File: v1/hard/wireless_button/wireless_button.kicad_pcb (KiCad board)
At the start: 2 copper layers, 82 x 56 mm, 21 parts, among them J1 USB_B_Micro, J2 RJ12, J3 Conn_01x01_Female, Q1 Q_PMOS_GSD, SW1 SW_Push, U1 STM32F103C8Tx, U2 CC1101_MOD, U3 OLED_0.91

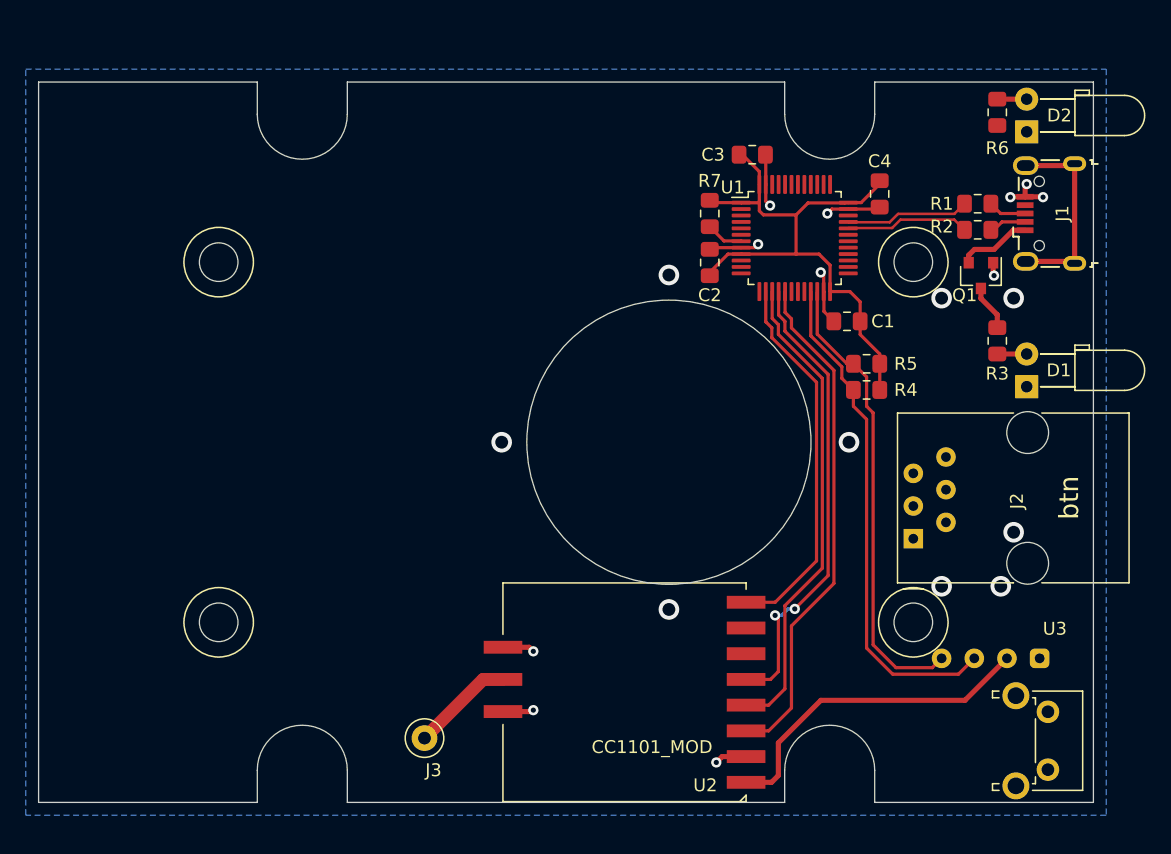
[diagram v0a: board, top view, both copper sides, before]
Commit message: Wireless button PCB updates. - added EEPROM - added connector for "pull-up" opto output - added overvoltage protection zener between source and gate of reverse protecting MOSFETs
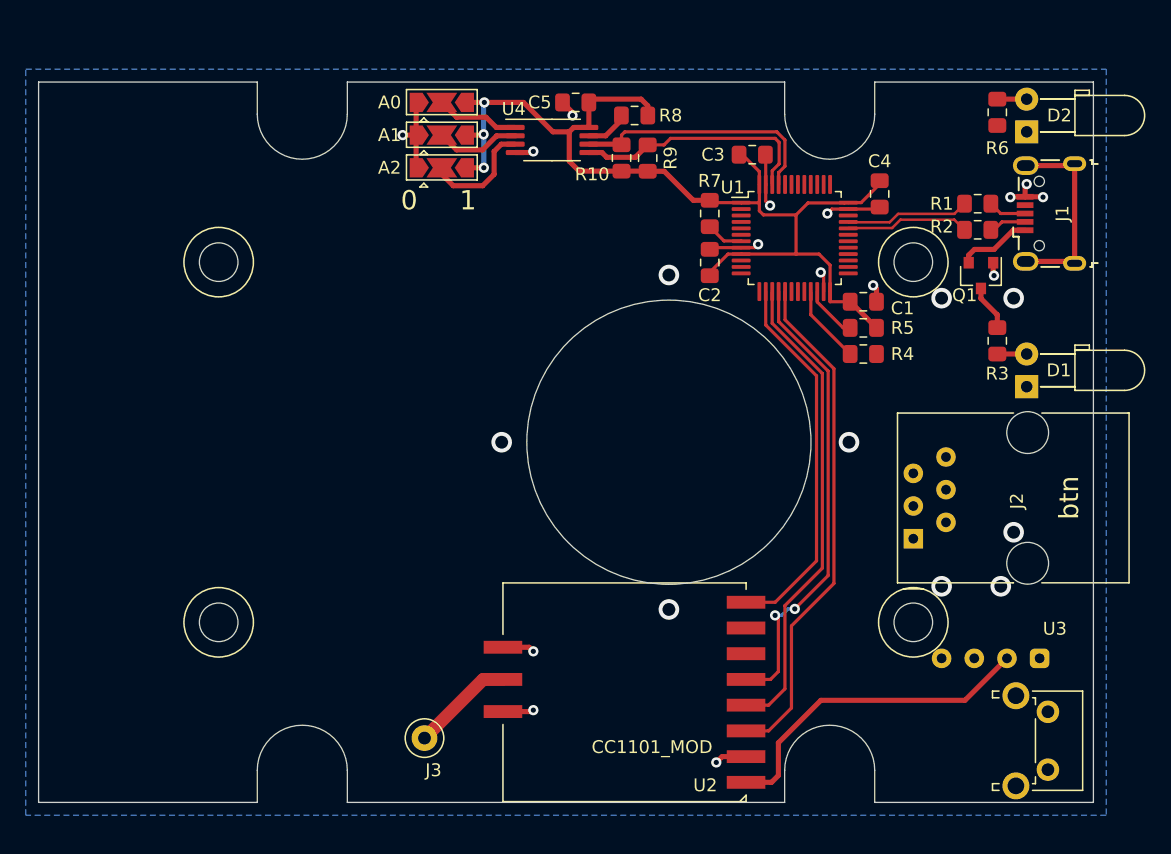
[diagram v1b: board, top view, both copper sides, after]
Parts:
- added C5: 0.1uF, Resistor_SMD:R_0805_2012Metric_Pad1.15x1.40mm_HandSolder, F.Cu at (100.8, 73.6)
- added JP1: A0, Jumper:SolderJumper-3_P2.0mm_Open_TrianglePad1.0x1.5mm, F.Cu at (90.3, 73.6)
- added JP2: A1, Jumper:SolderJumper-3_P2.0mm_Open_TrianglePad1.0x1.5mm, F.Cu at (90.3, 76.1)
- added JP3: A2, Jumper:SolderJumper-3_P2.0mm_Open_TrianglePad1.0x1.5mm, F.Cu at (90.3, 78.7)
- added R10: 4k7, Resistor_SMD:R_0805_2012Metric_Pad1.15x1.40mm_HandSolder, F.Cu at (104.3, 77.9)
- added R8: 4k7, Resistor_SMD:R_0805_2012Metric_Pad1.15x1.40mm_HandSolder, F.Cu at (105.3, 74.6)
- added R9: 4k7, Resistor_SMD:R_0805_2012Metric_Pad1.15x1.40mm_HandSolder, F.Cu at (106.3, 77.9)
- added U4: 24LC128, Package_SO:TSSOP-8_4.4x3mm_P0.65mm, F.Cu at (98.9, 76.5)
- moved R4 2.81 mm to (123.1, 93.1)
- moved R5 2.81 mm to (123.1, 91.1)
- moved C1 1.98 mm to (123.1, 89.1), turned to 0 degrees
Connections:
- U1 pad 45: Net-(U1-Pad45) -> /MEM_SCL
- U1 pad 46: Net-(U1-Pad46) -> /MEM_SDA
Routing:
- net +3V3: track 71.5 -> 106.9 mm, vias 0 -> 3
- net /OLED_SCL: track 39.2 -> 6.12 mm
- net /OLED_SDA: track 35.9 -> 4.20 mm
- net /MEM_SCL: track 0.00 -> 20.0 mm
- net /MEM_SDA: track 0.00 -> 19.2 mm
- net /MEM_A2: track 0.00 -> 8.96 mm
- net GND: track 28.6 -> 36.2 mm, vias 20 -> 24
- net /MEM_A1: track 0.00 -> 6.63 mm
- net /MEM_A0: track 0.00 -> 6.51 mm
- net /WP: track 0.00 -> 3.39 mm
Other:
- board text added: "0"
- board text added: "1"

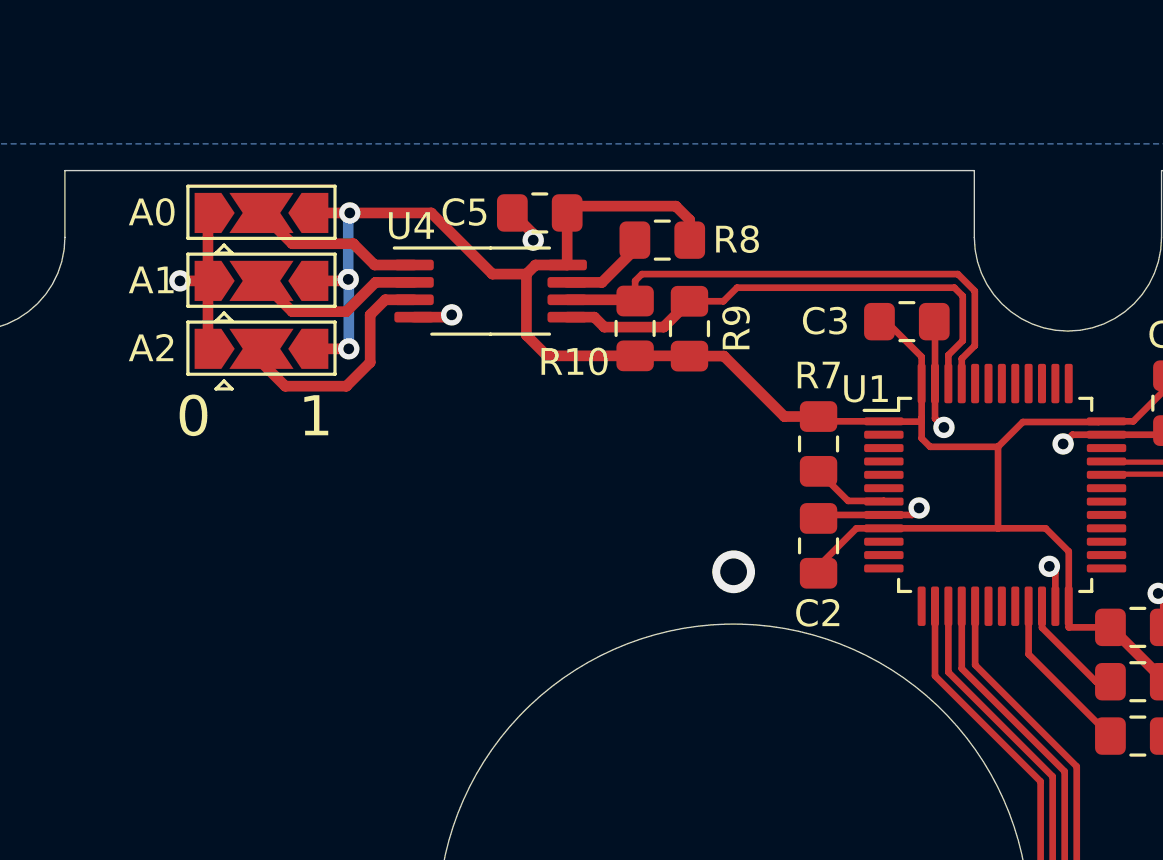
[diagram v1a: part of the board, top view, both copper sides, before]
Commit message: !!! Important. This is last commit before changing case from 1593L (aka BMD 60035) to G01B. !!! Many additions to wireless button. Came to conclusion that box is too small, mostly because of cuts on board sides. Also desided to drop idea powering from Li-batteriies and change to non rechangable +9V.
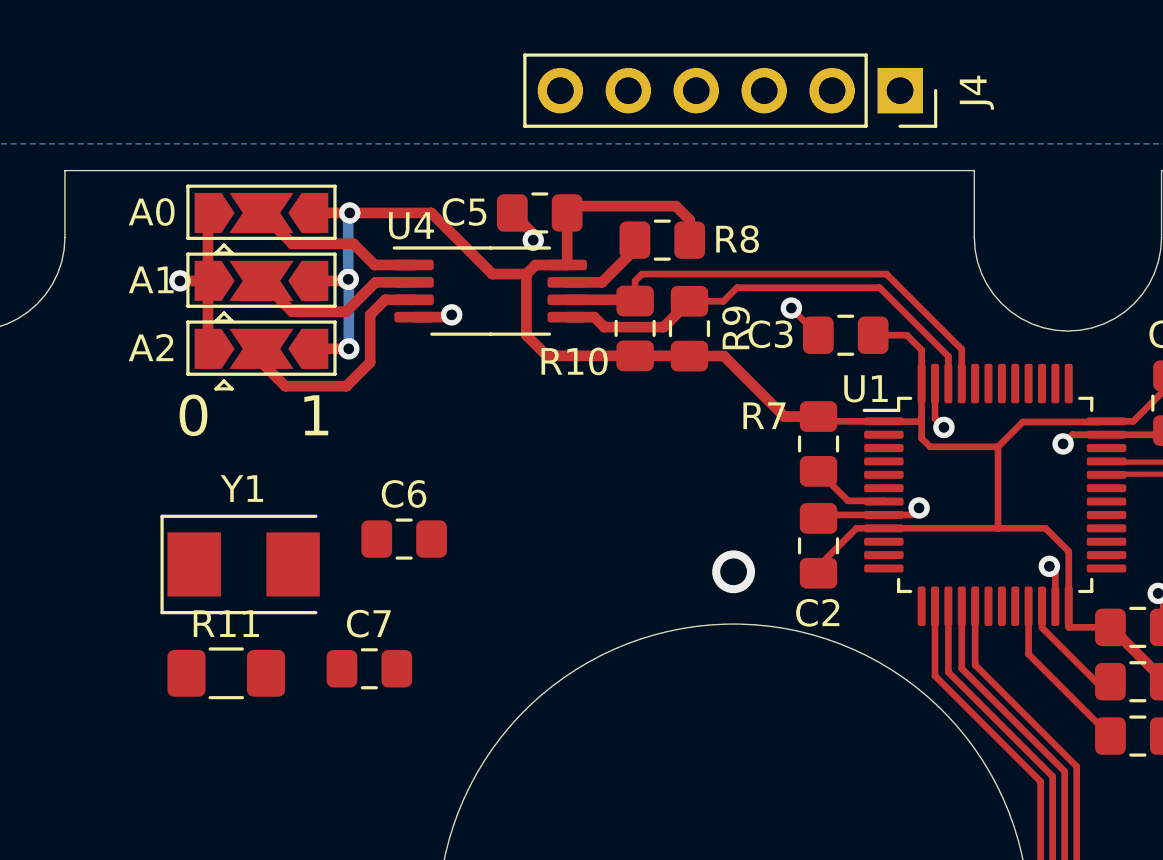
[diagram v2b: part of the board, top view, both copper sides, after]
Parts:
- added C6: 22pF, Resistor_SMD:R_0805_2012Metric_Pad1.15x1.40mm_HandSolder, F.Cu at (95.7, 85.8)
- added C7: 22pF, Resistor_SMD:R_0805_2012Metric_Pad1.15x1.40mm_HandSolder, F.Cu at (94.4, 90.6)
- added J4: Conn_01x06_Male, Connector_PinSocket_2.54mm:PinSocket_1x06_P2.54mm_Vertical, F.Cu at (114.2, 69.0)
- added R11: 1M, Resistor_SMD:R_1206_3216Metric_Pad1.42x1.75mm_HandSolder, F.Cu at (89.0, 90.8)
- added Y1: 8MHz, Crystal:Crystal_SMD_5032-2Pin_5.0x3.2mm, F.Cu at (89.7, 86.7)
- R7: value 47k -> 100k
- moved C3 2.34 mm to (112.2, 78.2), turned to 180 degrees
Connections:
- net /~RES renamed /NRST
- U1 pad 34: Net-(U1-Pad34) -> /SWDIO
- U1 pad 37: Net-(U1-Pad37) -> /SWCLK
- U1 pad 5: Net-(U1-Pad5) -> /OSCIN
- U1 pad 6: Net-(U1-Pad6) -> /OSCOUT
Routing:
- net /MEM_SDA: track 19.2 -> 17.1 mm
- net /MEM_SCL: track 20.0 -> 18.1 mm
- net GND: track 36.2 -> 35.3 mm, vias 24 -> 25

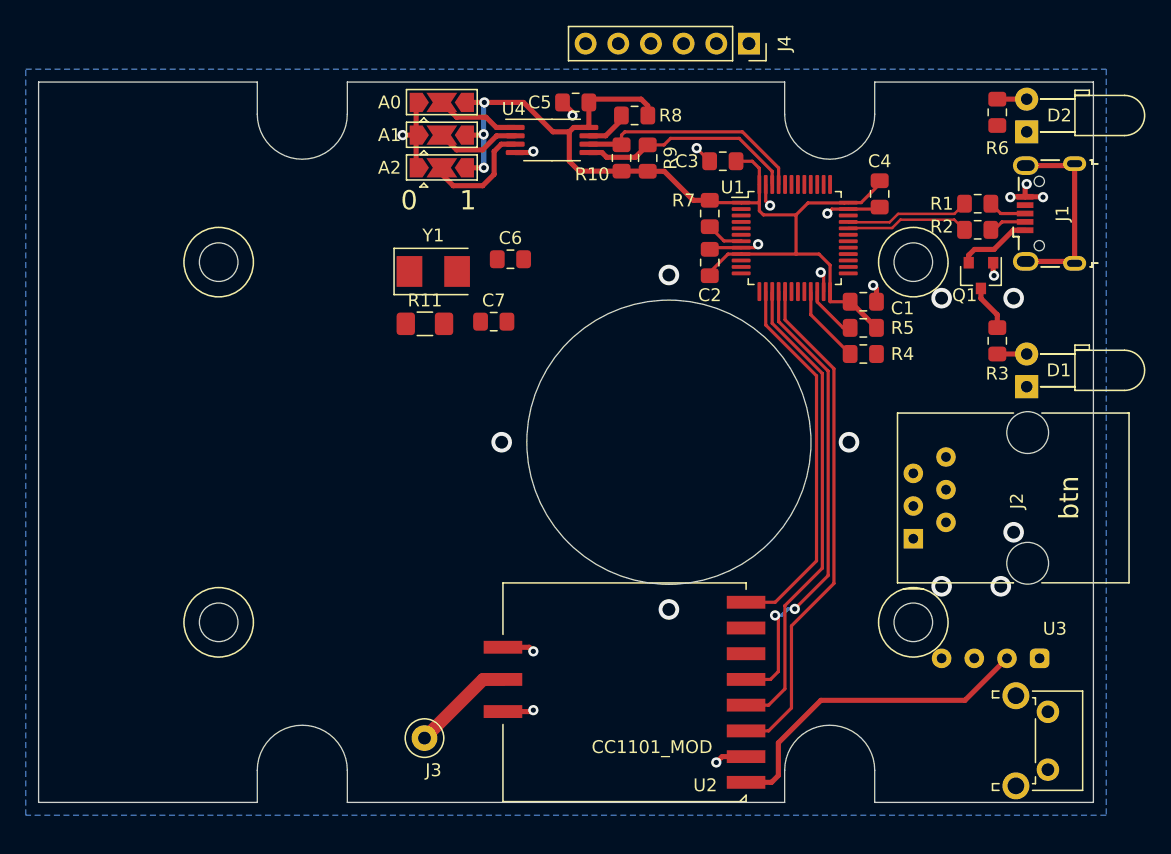
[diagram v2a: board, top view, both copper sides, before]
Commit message: Finished wireless button PCB v0.1. Added step-down converter to 3.3V from wide range input voltage. May contain serios mistakes, board is a prototype only.
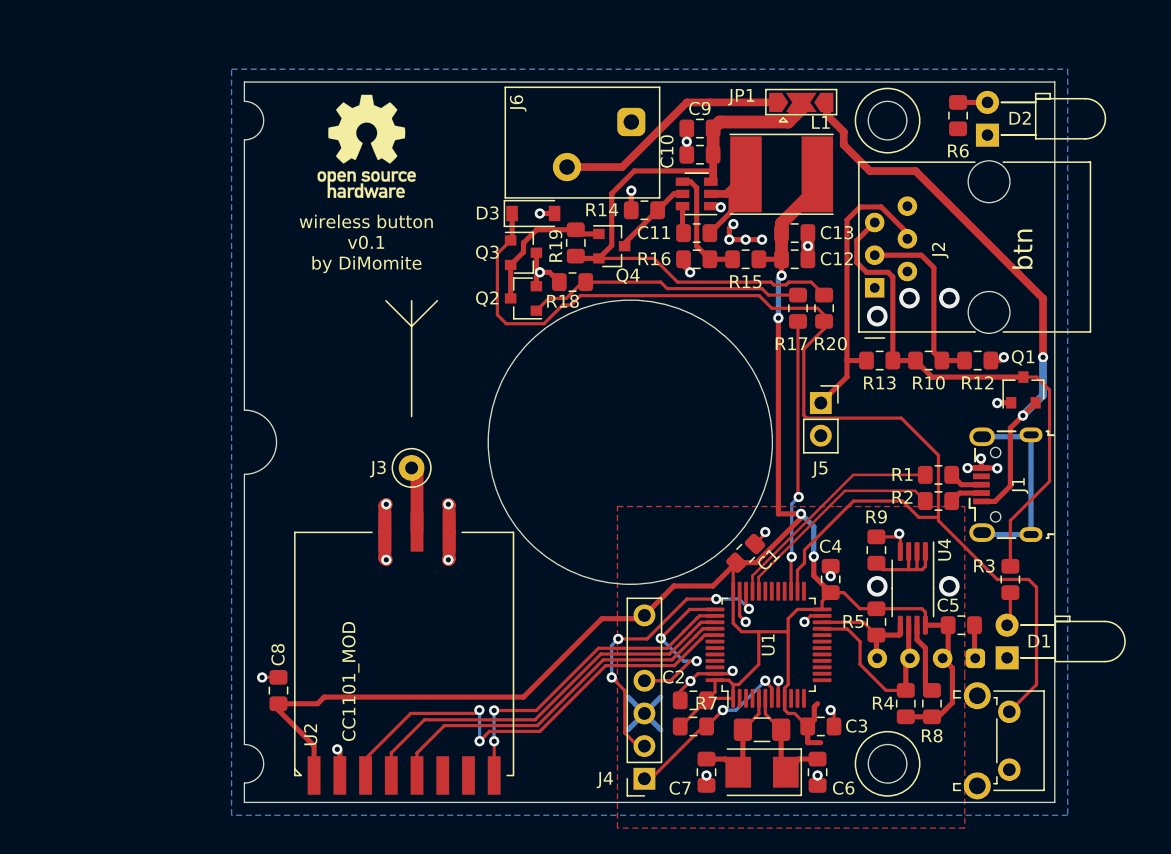
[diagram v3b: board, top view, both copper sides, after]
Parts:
- removed JP2: A1, Jumper:SolderJumper-3_P2.0mm_Open_TrianglePad1.0x1.5mm
- removed JP3: A2, Jumper:SolderJumper-3_P2.0mm_Open_TrianglePad1.0x1.5mm
- added C10: 10uF, Resistor_SMD:R_0805_2012Metric_Pad1.15x1.40mm_HandSolder, F.Cu at (110.4, 77.6)
- added C11: 0.1uF, Resistor_SMD:R_0805_2012Metric_Pad1.15x1.40mm_HandSolder, F.Cu at (110.2, 83.7)
- added C12: 22uF, Resistor_SMD:R_0805_2012Metric_Pad1.15x1.40mm_HandSolder, F.Cu at (117.8, 85.8)
- added C13: 22uF, Resistor_SMD:R_0805_2012Metric_Pad1.15x1.40mm_HandSolder, F.Cu at (117.8, 83.7)
- added C8: 0.1uF, Resistor_SMD:R_0805_2012Metric_Pad1.15x1.40mm_HandSolder, F.Cu at (77.6, 119.3)
- added C9: 10uF, Resistor_SMD:R_0805_2012Metric_Pad1.15x1.40mm_HandSolder, F.Cu at (110.4, 75.6)
- added D3: 4.8V, Diode_SMD:D_SOD-123, F.Cu at (97.5, 82.2)
- added J5: Conn_01x02_Female, Connector_PinSocket_2.54mm:PinSocket_1x02_P2.54mm_Vertical, F.Cu at (119.8, 97.0)
- added J6: Conn_01x02_Female, brbuttonsystem:Wago 250-3.5-2P-2, F.Cu at (105.1, 75.1)
- added L1: 4.7uH, Inductor_SMD:L_Taiyo-Yuden_NR-60xx_HandSoldering, F.Cu at (116.8, 79.2)
- added Q2: IRLML2803, Package_TO_SOT_SMD:SOT-23, F.Cu at (96.7, 88.8)
- added Q3: TP0610T, Package_TO_SOT_SMD:SOT-23, F.Cu at (96.7, 85.3)
- added Q4: TP0610T, Package_TO_SOT_SMD:SOT-23, F.Cu at (103.6, 84.8)
- added R12: 10k, Resistor_SMD:R_0805_2012Metric_Pad1.15x1.40mm_HandSolder, F.Cu at (132.0, 93.7)
- added R13: 4k7, Resistor_SMD:R_0805_2012Metric_Pad1.15x1.40mm_HandSolder, F.Cu at (124.4, 93.7)
- added R14: 100k, Resistor_SMD:R_0805_2012Metric_Pad1.15x1.40mm_HandSolder, F.Cu at (106.1, 82.0)
- added R15: 33.2k 1%, Resistor_SMD:R_0805_2012Metric_Pad1.15x1.40mm_HandSolder, F.Cu at (114.0, 85.8)
- added R16: 10k 1%, Resistor_SMD:R_0805_2012Metric_Pad1.15x1.40mm_HandSolder, F.Cu at (110.2, 85.8)
- added R17: 100k, Resistor_SMD:R_0805_2012Metric_Pad1.15x1.40mm_HandSolder, F.Cu at (118.0, 89.6)
- added R18: 100k, Resistor_SMD:R_0805_2012Metric_Pad1.15x1.40mm_HandSolder, F.Cu at (100.5, 87.6)
- added R19: 100k, Resistor_SMD:R_0805_2012Metric_Pad1.15x1.40mm_HandSolder, F.Cu at (100.8, 84.5)
- added R20: 10k, Resistor_SMD:R_0805_2012Metric_Pad1.15x1.40mm_HandSolder, F.Cu at (120.1, 89.6)
- added REF**: OSHW-Logo_7.5x8mm_SilkScreen, Symbol:OSHW-Logo_7.5x8mm_SilkScreen, F.Cu at (84.5, 77.0)
- added U5: TPS562200, Package_TO_SOT_SMD:SOT-23-6, F.Cu at (110.2, 80.7)
- JP1: value A0 -> Jumper_3_Bridged12
- R10, R9: value 4k7 -> 10k
- moved J4 57.7 mm to (106.1, 126.2), turned to 180 degrees
- moved R8 51.2 mm to (128.4, 120.3), turned to 90 degrees
- moved C5 50.5 mm to (130.7, 114.2), turned to 0 degrees
- moved Y1 46.6 mm to (115.2, 125.7), turned to 180 degrees
- moved C6 46.5 mm to (119.6, 125.7), turned to 270 degrees
- moved U4 44.7 mm to (127.0, 111.4), turned to 270 degrees
- moved C3 44.6 mm to (119.8, 122.1), turned to 0 degrees
- moved R11 41.0 mm to (115.2, 122.4)
- moved R7 39.9 mm to (109.9, 122.1), turned to 180 degrees
- moved C7 38.7 mm to (110.9, 125.7), turned to 270 degrees
- moved R9 35.3 mm to (124.1, 108.4), turned to 270 degrees
- moved U2 35.1 mm to (78.9, 125.9), turned to 90 degrees
- moved C2 34.1 mm to (109.9, 120.1), turned to 180 degrees
- moved U1 31.7 mm to (115.7, 115.7), turned to 90 degrees
- moved C4 30.2 mm to (120.6, 110.7), turned to 90 degrees
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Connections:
- net Net-(D1-Pad2) renamed /Reverse
- J2 pad 2: Net-(J2-Pad2) -> GND
- J2 pad 3: Net-(J2-Pad3) -> /MiddlePoint
- J2 pad 4: Net-(J2-Pad4) -> /ButtonPoint
- J2 pad 5: GND -> /PowInButt
- JP1 pad 1: GND -> +BATT
- JP1 pad 2: /MEM_A0 -> Net-(C10-Pad1)
- JP1 pad 3: +3V3 -> +5V
- Q1 pad 3: Net-(J2-Pad2) -> /PowInButt
- R10 pad 1: +3V3 -> /MiddlePoint
- R10 pad 2: /MEM_SCL -> /PowInButt
- R3 pad 1: Net-(J2-Pad2) -> /PowInButt
- R9 pad 1: +3V3 -> GND
- R9 pad 2: /MEM_SDA -> Net-(R9-Pad2)
- U1 pad 14: /WL_CS -> Net-(U1-Pad14)
- U1 pad 15: /WL_SCK -> Net-(U1-Pad15)
- U1 pad 16: /WL_MISO -> Net-(U1-Pad16)
- U1 pad 17: /WL_MOSI -> Net-(U1-Pad17)
- U1 pad 26: Net-(U1-Pad26) -> /power_switch
- U1 pad 27: Net-(U1-Pad27) -> /EN_PIN
- U1 pad 38: Net-(U1-Pad38) -> /WL_CS
- U1 pad 39: Net-(U1-Pad39) -> /WL_SCK
- U1 pad 40: Net-(U1-Pad40) -> /WL_MISO
- U1 pad 41: Net-(U1-Pad41) -> /WL_MOSI
- U4 pad 1: /MEM_A0 -> Net-(R9-Pad2)
- U4 pad 2: /MEM_A1 -> Net-(R9-Pad2)
- U4 pad 3: /MEM_A2 -> Net-(R9-Pad2)
- U4 pad 5: /MEM_SDA -> /OLED_SDA
- U4 pad 6: /MEM_SCL -> /OLED_SCL
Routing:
- net /power_switch: track 0.00 -> 97.1 mm
- net +3V3: track 107.0 -> 155.7 mm, vias 3 -> 4
- net Net-(C10-Pad1): track 0.00 -> 47.0 mm
- net /PowInButt: track 0.00 -> 41.5 mm
- net +5V: track 5.78 -> 44.1 mm, vias 0 -> 2
- net GND: track 35.3 -> 64.0 mm, vias 25 -> 38
- net /SWDIO: track 0.00 -> 23.1 mm, vias 0 -> 4
- net /ButtonPoint: track 0.00 -> 23.0 mm
- net Net-(Q2-Pad1): track 0.00 -> 21.7 mm
- net /EN_PIN: track 0.00 -> 21.2 mm, vias 0 -> 2
- net +BATT: track 0.00 -> 18.3 mm
- net /MEM_SCL: track 18.1 -> 0.00 mm
- net /MEM_SDA: track 17.1 -> 0.00 mm
- net /MiddlePoint: track 0.00 -> 14.2 mm
- net /SWCLK: track 0.00 -> 13.4 mm, vias 0 -> 2
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- added copper zone on F.Cu, net +3V3
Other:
- board size 82 x 56 mm -> 63 x 56 mm
- board text added: "wireless button v0.1 by DiMomite"
- board text removed: "0"
- board text removed: "1"
- board text removed: "25mm is a size of LiPo battery pack For reference"
